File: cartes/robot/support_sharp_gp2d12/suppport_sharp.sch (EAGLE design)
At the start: 33 parts, among them U1 SN65HVD08D, X1 5V_INPUT, X2 12V_INPUT

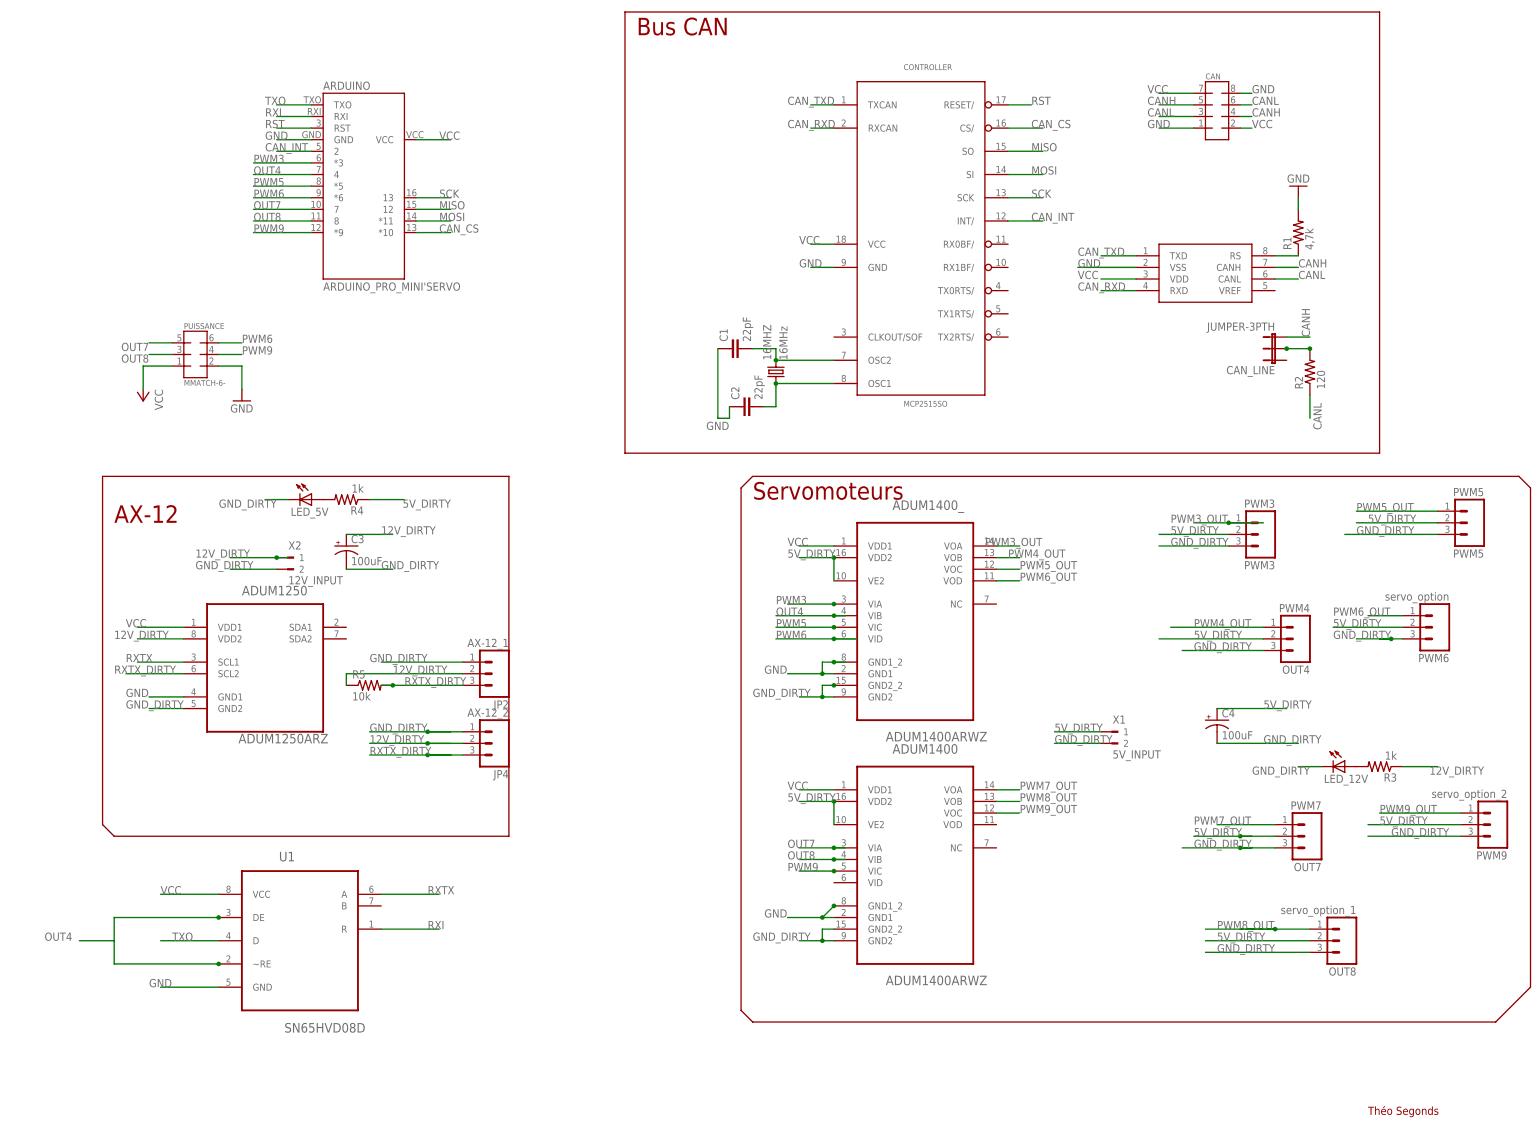
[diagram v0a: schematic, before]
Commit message: Ajout carte support sharp
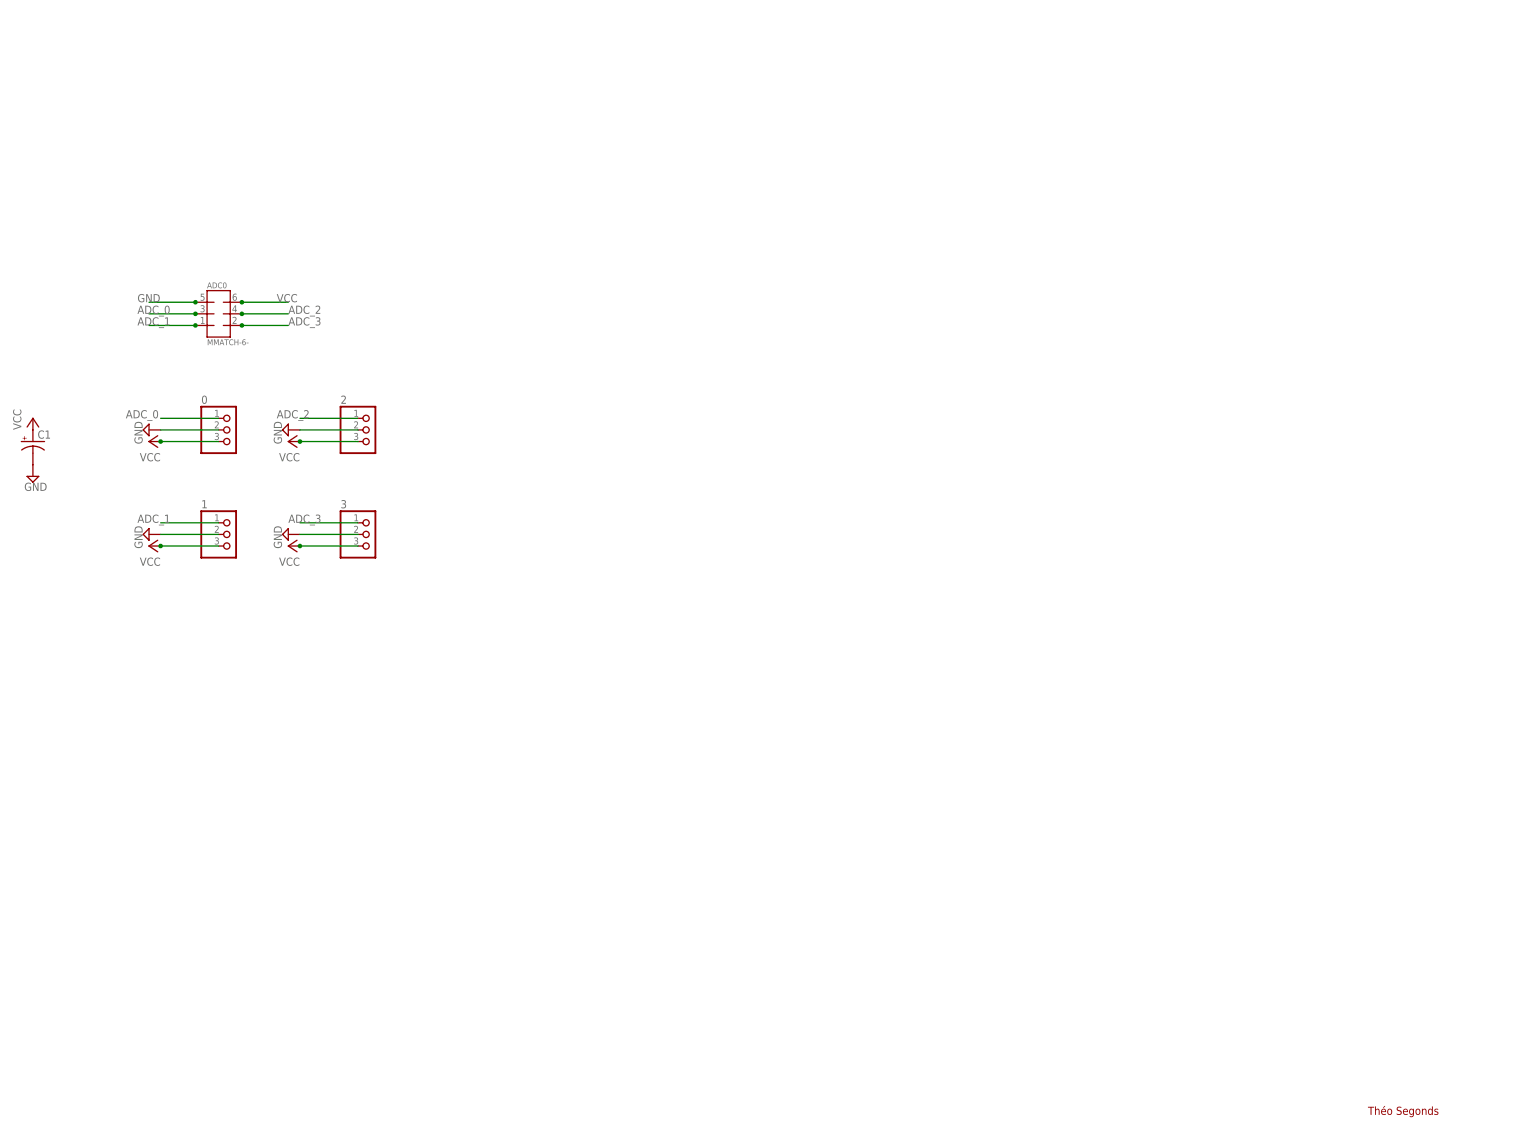
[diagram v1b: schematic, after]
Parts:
- removed 16MHZ: 16MHz, adafruit:CRYSTALHC49S
- removed ADUM1250: ADUM1250ARZ, Analog Devices_By_element14_Batch_1:ADUM1250ARZ
- removed ADUM1400, ADUM1400_: ADUM1400ARWZ, Analog Devices_By_element14_Batch_1:ADUM1400ARWZ
- removed ARDUINO: ARDUINO_PRO_MINI'SERVO, can_bus_servo:ARDUINO_PRO_MINI'SERVO
- removed C2: 22pF, SparkFun-Capacitors:CAP0805
- removed C3, C4: 100uF, SparkFun-Capacitors:CAP_POLPTH1
- removed CAN: (no value), jt-con-micromatch:MMATCH-8-PTH
- removed CAN_LINE: JUMPER-3PTH, SparkFun-Passives:JUMPER-3PTH
- removed CONTROLLER: MCP2515SO, MCP2515_MT:MCP2515SO
- removed JP2: AX-12_1, SparkFun-Connectors:M03POLAR
- removed JP4: AX-12_2, SparkFun-Connectors:M03POLAR
- removed LED_12V, LED_5V: (no value), adafruit:LEDCHIPLED_0805
- removed OUT4: PWM4, SparkFun-Connectors:M03PTH
- removed OUT7: PWM7, SparkFun-Connectors:M03PTH
- removed OUT8: servo_option_1, SparkFun-Connectors:M03PTH
- removed PUISSANCE: MMATCH-6-, jt-con-micromatch:MMATCH-6-
- removed PWM3: PWM3, SparkFun-Connectors:M03PTH
- removed PWM5: PWM5, SparkFun-Connectors:M03PTH
- removed PWM6: servo_option, SparkFun-Connectors:M03PTH
- removed PWM9: servo_option_2, SparkFun-Connectors:M03PTH
- removed R1: 4,7k, SparkFun-Passives:RESISTOR0805-RES
- removed R2: 120, SparkFun-Passives:RESISTOR0805-RES
- removed R3, R4: 1k, SparkFun-Passives:RESISTOR0805-RES
- removed R5: 10k, SparkFun-Passives:RESISTOR0805-RES
- removed TRANSCEIVER: MCP2551, SparkFun-DigitalIC:MCP2551
- removed U1: SN65HVD08D, Texas Instruments_By_element14_Batch_1:SN65HVD08D
- removed X1: 5V_INPUT, con-weidmueller-sl35:90-2
- removed X2: 12V_INPUT, con-weidmueller-sl35:90-2
- added 0, 1, 2, 3: (no value), pinhead:PINHD-1X3
- added ADC0: MMATCH-6-, jt-con-micromatch:MMATCH-6-
- C1: value 22pF -> (none); device SparkFun-Capacitors:CAP0805 -> SparkFun-Passives:CAP_POLPTH1; MF AVX -> (none); MPN 08055A220JAT2A -> (none); OC_FARNELL 2280675RL -> (none)
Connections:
- removed net 12V_DIRTY: ADUM1250.VDD2, C3.+, JP2.2, JP4.2, R3.1, R5.1, X2.1
- removed net 5V_DIRTY: ADUM1400.VDD2, ADUM1400.VE2, ADUM1400_.VDD2, ADUM1400_.VE2, C4.+, OUT4.2, OUT7.2, OUT8.2, PWM3.2, PWM5.2, PWM6.2, PWM9.2, R4.1, X1.1
- removed net CANH: CAN.4, CAN.5, CAN_LINE.3, TRANSCEIVER.CANH
- removed net CANL: CAN.3, CAN.6, R2.1, TRANSCEIVER.CANL
- removed net CAN_CS: ARDUINO.*10, CONTROLLER.CS/
- removed net CAN_INT: ARDUINO.2, CONTROLLER.INT/
- removed net CAN_RXD: CONTROLLER.RXCAN, TRANSCEIVER.RXD
- removed net CAN_TXD: CONTROLLER.TXCAN, TRANSCEIVER.TXD
- removed net GND_DIRTY: ADUM1250.GND2, ADUM1400.GND2, ADUM1400.GND2_2, ADUM1400_.GND2, ADUM1400_.GND2_2, C3.-, C4.-, JP2.1, JP4.1, LED_12V.C, LED_5V.C, OUT4.3, OUT7.3, OUT8.3, PWM3.3, PWM5.3, PWM6.3, PWM9.3, X1.2, X2.2
- removed net MISO: ARDUINO.12, CONTROLLER.SO
- removed net MOSI: ARDUINO.*11, CONTROLLER.SI
- removed net N$2: 16MHZ.2, C1.2, CONTROLLER.OSC2
- removed net N$3: 16MHZ.1, C2.2, CONTROLLER.OSC1
- removed net N$4: LED_12V.A, R3.2
- removed net N$5: R1.1, TRANSCEIVER.RS
- removed net N$6: LED_5V.A, R4.2
- removed net N$7: CAN_LINE.2, R2.2
- removed net OUT4: ADUM1400_.VIB, ARDUINO.4, U1.DE, U1.~RE
- removed net OUT7: ADUM1400.VIA, ARDUINO.7, PUISSANCE.7
- removed net OUT8: ADUM1400.VIB, ARDUINO.8, PUISSANCE.5
- removed net PWM3: ADUM1400_.VIA, ARDUINO.*3
- removed net PWM3_OUT: ADUM1400_.VOA, PWM3.1
- removed net PWM4_OUT: ADUM1400_.VOB, OUT4.1
- removed net PWM5: ADUM1400_.VIC, ARDUINO.*5
- removed net PWM5_OUT: ADUM1400_.VOC, PWM5.1
- removed net PWM6: ADUM1400_.VID, ARDUINO.*6, PUISSANCE.8
- removed net PWM6_OUT: ADUM1400_.VOD, PWM6.1
- removed net PWM7_OUT: ADUM1400.VOA, OUT7.1
- removed net PWM8_OUT: ADUM1400.VOB, OUT8.1
- removed net PWM9: ADUM1400.VIC, ARDUINO.*9, PUISSANCE.6
- removed net PWM9_OUT: ADUM1400.VOC, PWM9.1
- removed net RST: ARDUINO.RST, CONTROLLER.RESET/
- removed net RXI: ARDUINO.RXI, U1.R
- removed net RXTX: ADUM1250.SCL1, U1.A
- removed net RXTX_DIRTY: ADUM1250.SCL2, JP2.3, JP4.3, R5.2
- removed net SCK: ARDUINO.13, CONTROLLER.SCK
- removed net TXO: ARDUINO.TXO, U1.D
- new net ADC_0: 0.1, ADC0.5
- new net ADC_1: 1.1, ADC0.3
- new net ADC_2: 2.1, ADC0.6
- new net ADC_3: 3.1, ADC0.4
- net GND: now also 0.2, 1.2, 2.2, 3.2, ADC0.7, C1.-; no longer ADUM1250.GND1, ADUM1400.GND1, ADUM1400.GND1_2, ADUM1400_.GND1, ADUM1400_.GND1_2, ARDUINO.GND, C1.1, C2.1, CAN.1, CAN.8, CONTROLLER.GND, PUISSANCE.4, R1.2, TRANSCEIVER.VSS, U1.GND
- net VCC: now also 0.3, 1.3, 2.3, 3.3, ADC0.8, C1.+; no longer ADUM1250.VDD1, ADUM1400.VDD1, ADUM1400_.VDD1, ARDUINO.VCC, CAN.2, CAN.7, CONTROLLER.VCC, PUISSANCE.3, TRANSCEIVER.VDD, U1.VCC
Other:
- note removed: "AX-12"
- note removed: "Bus CAN"
- note removed: "Servomoteurs"
